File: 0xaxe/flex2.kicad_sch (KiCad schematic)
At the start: 89 parts, among them U14 MCP1824T-1802E, U6001 25MHz, U6003 NCP114ASN080T1G, U6004 ADUM141E0BRZ-RL7, U6005 +0V8, U6006 +0V8, U6007 BM1366_mode1, U6008 +0V8, U6009 +0V8, U6010 +0V8, U6011 +0V8, U6012 +0V8, U6013 +0V8, U6014 +0V8, U6015 +0V8, U6016 +0V8, U6017 +0V8, U6018 BM1366_mode1, U6019 +0V8, U6020 +0V8, U6021 BM1366_mode1, U6022 +0V8, U6024 +0V8, U6025 BM1366_mode1, U6026 +0V8

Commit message: rev1.2
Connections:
- net +5V renamed +6.5V
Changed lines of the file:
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@@
 	)
 	(symbol
-		(lib_id "power:+5V")
-		(at 86.36 175.26 0)
-		(unit 1)
-		(exclude_from_sim no)
-		(in_bom yes)
-		(on_board yes)
-		(dnp no)
-		(fields_autoplaced yes)
-		(property "Reference" "#PWR0142"
-			(at 86.36 179.07 0)
-			(effects
-				(font
-					(size 1.27 1.27)
-				)
-				(hide yes)
-			)
-		)
-		(property "Value" "+5V"
-			(at 86.36 170.18 0)
-			(effects
-				(font
-					(size 1.27 1.27)
-				)
-			)
-		)
-		(property "Footprint" ""
-			(at 86.36 175.26 0)
-			(effects
-				(font
-					(size 1.27 1.27)
-				)
-				(hide yes)
-			)
-		)
-		(property "Datasheet" ""
-			(at 86.36 175.26 0)
-			(effects
-				(font
-					(size 1.27 1.27)
-				)
-				(hide yes)
-			)
-		)
-		(property "Description" "Power symbol creates a global label with name \"+5V\""
-			(at 86.36 175.26 0)
-			(effects
-				(font
-					(size 1.27 1.27)
-				)
-				(hide yes)
-			)
-		)
-		(pin "1"
-		)
-		(instances
-			(project "0xaxe"
-				(path "/e63e39d7-6ac0-4ffd-8aa3-1841a4541b55/84d407d0-bd71-403d-bc5c-679b63d0a5ac/685a8d0d-4dc2-4a68-9e2a-a2b107c3af74"
-					(reference "#PWR0142")
-					(unit 1)
-				)
-			)
-		)
-	)
-	(symbol
 		(lib_id "Device:C")
 		(at 275.59 231.14 0)
@@
 					(unit 1)
 				)
+			)
+		)
+	)
+	(symbol
+		(lib_id "mylib7:+6.5V")
+		(at 86.36 175.26 0)
+		(unit 1)
+		(exclude_from_sim no)
+		(in_bom yes)
+		(on_board yes)
+		(dnp no)
+		(fields_autoplaced yes)
+		(property "Reference" "#PWR0142"
+			(at 86.36 179.07 0)
+			(effects
+				(font
+					(size 1.27 1.27)
+				)
+				(hide yes)
+			)
+		)
+		(property "Value" "+6.5V"
+			(at 86.36 170.18 0)
+			(effects
+				(font
+					(size 1.27 1.27)
+				)
+			)
+		)
+		(property "Footprint" ""
+			(at 86.36 175.26 0)
+			(effects
+				(font
+					(size 1.27 1.27)
+				)
+				(hide yes)
+			)
+		)
+		(property "Datasheet" ""
+			(at 86.36 175.26 0)
+			(effects
+				(font
+					(size 1.27 1.27)
+				)
+				(hide yes)
+			)
+		)
+		(property "Description" ""
+			(at 86.36 175.26 0)
+			(effects
+				(font
+					(size 1.27 1.27)
+				)
+				(hide yes)
+			)
+		)
+		(pin "1"
+		)
+		(instances
+			(project "0xaxe"
+				(path "/e63e39d7-6ac0-4ffd-8aa3-1841a4541b55/84d407d0-bd71-403d-bc5c-679b63d0a5ac/685a8d0d-4dc2-4a68-9e2a-a2b107c3af74"
+					(reference "#PWR0142")
+					(unit 1)
+				)

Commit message: op levelshifter
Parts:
- removed C6010, C6011: 100n, Capacitor_SMD:C_0805_2012Metric, symbol Device:C
- removed U6004: ADUM141E0BRZ-RL7, Package_SO:SOIC-16_3.9x9.9mm_P1.27mm, symbol Isolator:ADuM1411
- added C107: 0.1uF, Capacitor_SMD:C_0805_2012Metric, symbol Device:C
- added C108: 1uF, Capacitor_SMD:C_0805_2012Metric, symbol Device:C
- added C284, C285, C286, C287: 100pF, Capacitor_SMD:C_0805_2012Metric, symbol Device:C
- added R71, R74, R77, R78, R79, R82, R85, R86, R87: 1k, Resistor_SMD:R_0805_2012Metric, symbol Device:R
- added R72, R73, R75, R76, R80, R81, R83, R84: 10k, Resistor_SMD:R_0805_2012Metric, symbol Device:R
- added U41: TLV3544, Package_SO:SOIC-14_3.9x8.7mm_P1.27mm, symbol bitaxe:TLV3544
- renumbered C6003 to C100, C6004 to C101, C6005 to C102, C6006 to C103, C6007 to C104, C6009 to C106, C6012 to C109, C6013 to C110, C6014 to C111, C6015 to C112, C6016 to C113, C6017 to C114, C6018 to C115, C6019 to C116, C6020 to C117, C6021 to C118, C6022 to C119, C6023 to C120, C6024 to C121, C6025 to C122, C6026 to C123, C6027 to C124, C6028 to C125, C6029 to C126, C6030 to C127, C6031 to C128, C6032 to C129, C6033 to C130, C6034 to C131, C6035 to C132, C6036 to C133, C6037 to C134, C6038 to C135, C6039 to C136, C6040 to C137, C6041 to C138, C6042 to C139, C6043 to C140, C6044 to C141, C6045 to C142, C6046 to C143, C6047 to C144, C6048 to C145, C6049 to C146, C6050 to C147, C6051 to C148, C6052 to C149, C6053 to C150, C6054 to C151, C6055 to C152, C6057 to C153, C6058 to C154, C6059 to C155, C6060 to C156, C6061 to C157, C6002 to C99, R6003 to R44, R6004 to R45, R6005 to R46, R6006 to R47, U6001 to U38, U6003 to U40, U6005 to U42, U6006 to U43, U6007 to U44, U6008 to U45, U6009 to U46, U6010 to U47, U6011 to U48, U6012 to U49, U6013 to U50, U6014 to U51, U6015 to U52, U6016 to U53, U6017 to U54, U6018 to U55, U6019 to U56, U6020 to U57, U6021 to U58, U6022 to U59, U6024 to U60, U6025 to U61, U6026 to U62
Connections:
- net +6.5V: now also C107.2, C108.2, U41.4 (V+)
- net BI: now also R84.1
- net CI: now also R73.1
- net GND_1: now also R71.2, R74.2, R79.2, R82.2
- net NRSTI: now also R76.1
- net NRSTO: now also C285.2, R78.1, U41.7; no longer U44.5 (NRSTO)
- net RO: now also R87.1
- net CLKI renamed I_CLKI
- new net: R83.2, R84.2, U41.10 (+)
- new net: C287.1, R82.1, R86.2, U41.9 (-)
- new net: C286.1, R79.1, R85.2, U41.13 (-)
- new net: C286.2, R85.1, R87.2, U41.14
- new net: C285.1, R74.1, R78.2, U41.6 (-)
- new net: R80.2, R81.2, U41.12 (+)
- new net: R72.1, R73.2, U41.3 (+)
- new net: C284.1, R71.1, R77.2, U41.2 (-)
- new net: R75.2, R76.2, U41.5 (+)
- new net BI_1: C287.2, R86.1, U41.8
- new net CI_1: C284.2, R77.1, U41.1
- new net GND: C107.1, C108.1, U41.11 (V-)
- new net I_NRSTI: U44.5 (NRSTI)
- new net RO_1: R81.1
- new net VDD_1: R72.2, R75.1, R83.1
- new net VDD_REF_I: R80.1
- no-connect marks 21 -> 19
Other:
- note added: "+0V8 LDO"
- note added: "+1V8 LDO"
- note added: "25MHz Osc for CLKI"
- note added: "Levelshift of input signals to own voltage domain"
- note added: "OPAMP Bypass"
- moved on the sheet: C100, C101, C102, C103, C104, C106, C109, C110, C111, C112, C113, C114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

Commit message: General Update
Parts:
- U42, U43, U45, U46, U47, U48, U49, U50, U51, U52, U53, U54, U56, U57, U59, U60, U62: value +0V8 -> +0V8_1
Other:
- note added: "+0V8_1 LDO"
- note removed: "+0V8 LDO"
- moved on the sheet: C110, C111, C113, C114, C115, C116, C118, C119, C120, C121, C122, C124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

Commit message: fixed couple of things
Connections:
- net BI is gone; now on net BI_1: R84.1
- net CI is gone; now on net CI_1: R73.1
- net NRSTO is gone; now on net NRSTO_1: C285.2, R78.1, U41.7
- net RO is gone; now on net RO_1: R87.1
- net VDD_1 is gone; now on net +1V2_1: R72.2, R75.1, R83.1
- net BI_1: no longer C287.2, R86.1, U41.8
- net CI_1: no longer C284.2, R77.1, U41.1
- net RO_1: no longer R81.1
- net BO renamed BO_1
- net CO renamed CO_1
- net I_BI renamed I_BI_1
- net I_BI_1: now also C287.2, R86.1, U41.8
- net I_CI renamed I_CI_1
- net I_CI_1: now also C284.2, R77.1, U41.1
- net I_CLKI renamed I_CLKI_1
- net I_NRSTI renamed NRSTO_1
- net I_RO renamed I_RO_1
- net I_RO_1: now also R81.1
- net NRSTI renamed NRSTI_1
- net RI renamed RI_1
- net VDD_REF_I renamed VDD_REF_I_1
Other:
- moved on the sheet: C100, C101, C103, C107, C108, C110, C111, C113, C114, C115, C116, C117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

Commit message: Layout update
Layout with OP
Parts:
- removed R71, R74, R77, R78, R79, R82, R85, R86, R87: 1k, Resistor_SMD:R_0805_2012Metric, symbol Device:R
- removed R72, R73, R75, R76, R80, R81, R83, R84: 10k, Resistor_SMD:R_0805_2012Metric, symbol Device:R
- added RN5, RN6, RN7, RN8: 10k, EXB-28V103JX:EXB28V_PAN, symbol Device:R_Network04_Split
- U44, U55, U58, U61: footprint qaxe:BM1366 -> bitvein:BM1366
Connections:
- net +1V2_1: now also RN5.8 (R4.2), RN6.1 (R1), RN8.4 (R2.2)
- net BI_1: now also RN8.5 (R2.2)
- net CI_1: now also RN5.1 (R1)
- net GND_1: now also RN5.5 (R2.2), RN6.4 (R2.2), RN7.4 (R2.2), RN8.1 (R1)
- net I_BI_1: now also RN8.8 (R4.2)
- net I_CI_1: now also RN5.4 (R2.2)
- net I_RO_1: now also RN7.8 (R4.2)
- net NRSTI_1: now also RN6.8 (R4.2)
- net NRSTO_1: now also RN6.5 (R2.2)
- net RO_1: now also C286.2, U41.14, RN7.5 (R2.2)
- net VDD_REF_I_1: now also RN7.1 (R1)
- net at U41.10 (+): now also RN8.3 (R2.2), RN8.6 (R3.2)
- net at C287.1, U41.9 (-): now also RN8.2 (R1.2), RN8.7 (R2.2)
- net at C286.1, U41.13 (-): now also RN7.3 (R2.2), RN7.6 (R3.2)
- net at C285.1, U41.6 (-): now also RN6.3 (R2.2), RN6.6 (R3.2)
- net at U41.12 (+): now also RN7.2 (R1.2), RN7.7 (R2.2)
- net at U41.3 (+): now also RN5.2 (R1.2), RN5.7 (R2.2)
- net at C284.1, U41.2 (-): now also RN5.3 (R2.2), RN5.6 (R3.2)
- net at U41.5 (+): now also RN6.2 (R1.2), RN6.7 (R2.2)

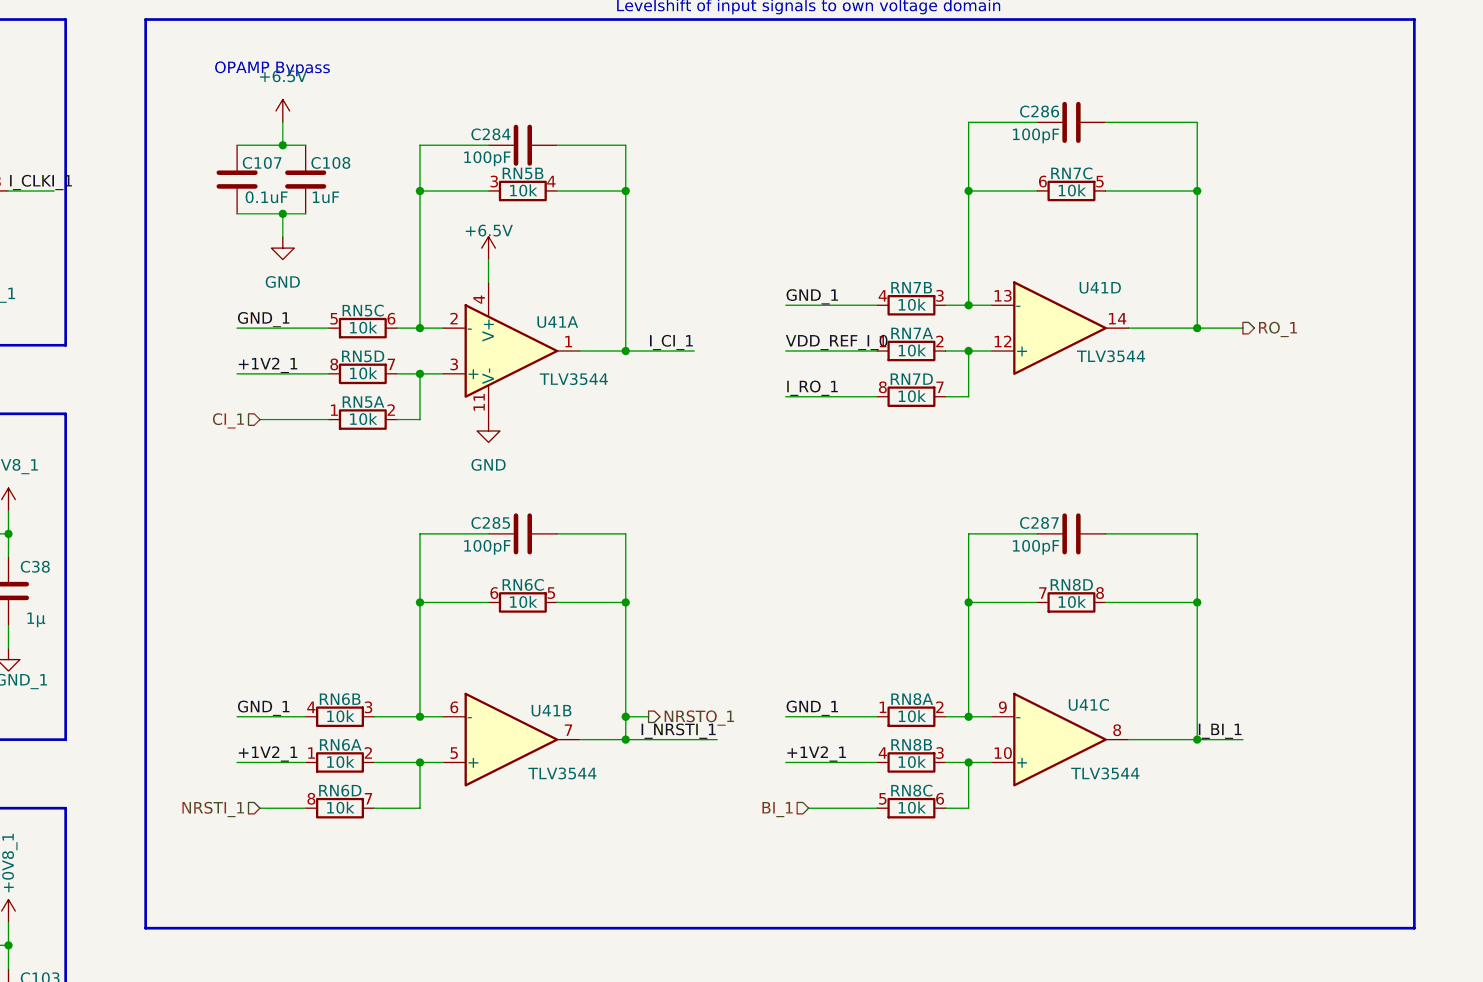
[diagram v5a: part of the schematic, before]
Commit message: fixed level shifter, added optional headers for future extensions
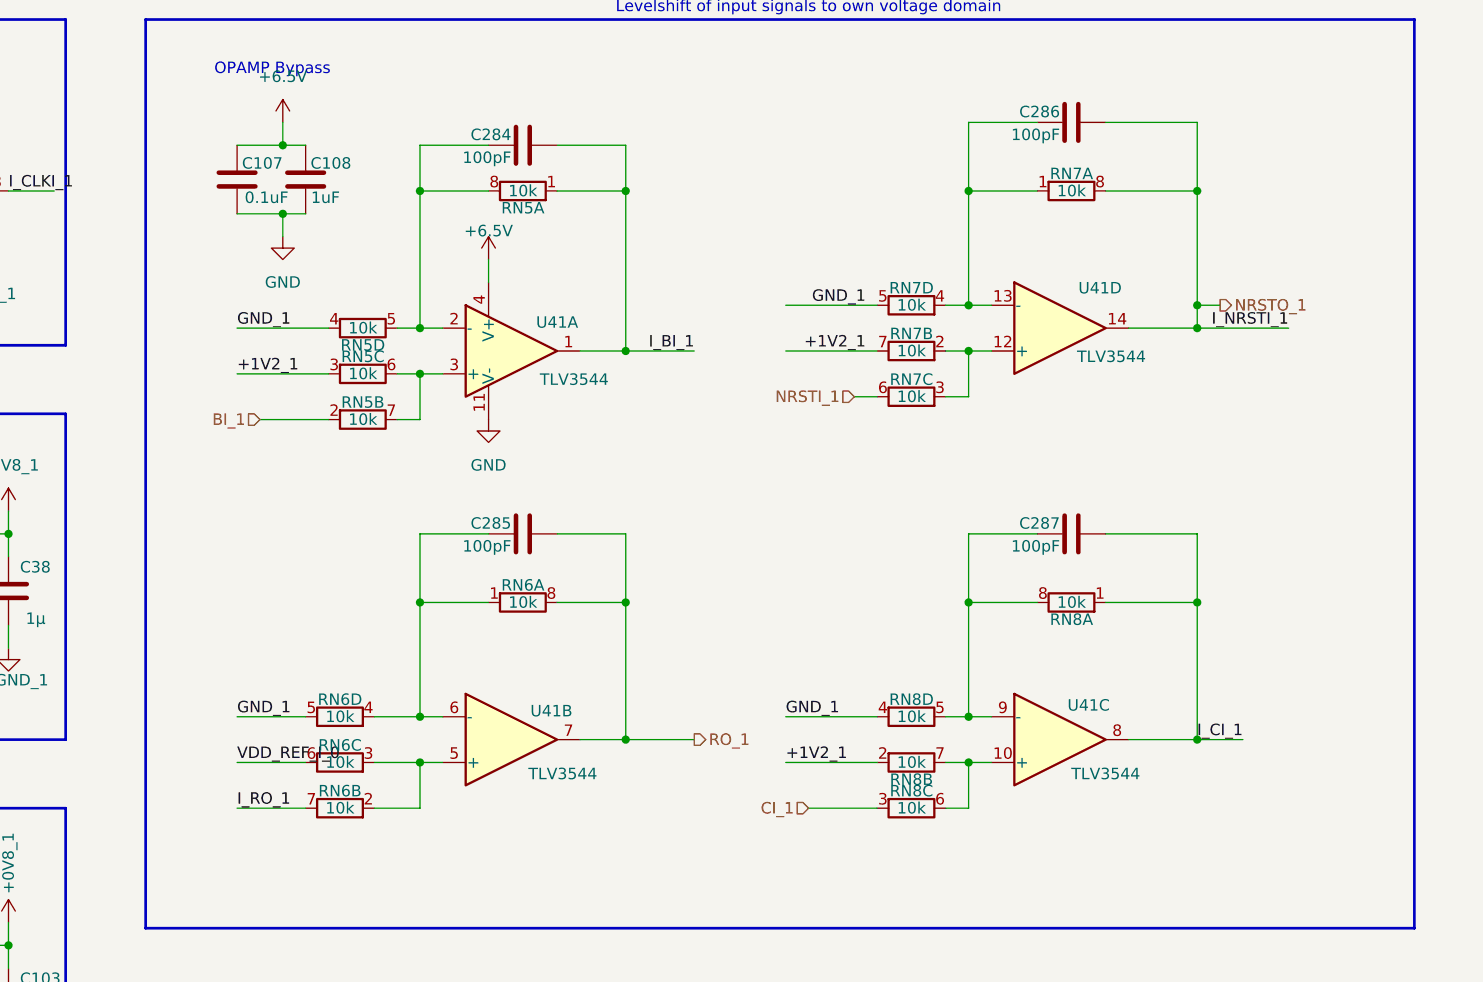
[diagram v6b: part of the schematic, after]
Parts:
- RN5, RN6, RN7, RN8: footprint EXB-28V103JX:EXB28V_PAN -> Resistor_SMD:R_Array_Convex_4x0603; symbol Device:R_Network04_Split -> mylib7:R_Network04_Split_SMD
- U44, U55, U58, U61: footprint bitvein:BM1366 -> myfootprints:BM1366-user1-soldermask
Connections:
- net +1V2_1: now also RN5.3 (R3.1), RN7.7 (R2.2), RN8.2 (R2.1); no longer RN5.8 (R4.2), RN6.1 (R1), RN8.4 (R2.2)
- net BI_1: now also RN5.2 (R2.1); no longer RN8.5 (R2.2)
- net CI_1: now also RN8.3 (R3.1); no longer RN5.1 (R1)
- net GND_1: now also RN5.4 (R4.1), RN6.5 (R4.2), RN7.5 (R4.2), RN8.4 (R4.1); no longer RN5.5 (R2.2), RN6.4 (R2.2), RN7.4 (R2.2), RN8.1 (R1)
- net I_BI_1: now also C284.2, RN5.1 (R1.1), U41.1; no longer C287.2, RN8.8 (R4.2), U41.8
- net I_CI_1: now also C287.2, RN8.1 (R1.1), U41.8; no longer C284.2, RN5.4 (R2.2), U41.1
- net I_RO_1: now also RN6.7 (R2.2); no longer RN7.8 (R4.2)
- net NRSTI_1: now also RN7.6 (R3.2); no longer RN6.8 (R4.2)
- net NRSTO_1: now also C286.2, RN7.8 (R1.2), U41.14; no longer C285.2, RN6.5 (R2.2), U41.7
- net RO_1: now also C285.2, RN6.8 (R1.2), U41.7; no longer C286.2, RN7.5 (R2.2), U41.14
- net VDD_REF_I_1: now also RN6.6 (R3.2); no longer RN7.1 (R1)
- net at RN8.6 (R3.2), U41.10 (+): now also RN8.7 (R2.2); no longer RN8.3 (R2.2)
- net at C287.1, U41.9 (-): now also RN8.5 (R4.2), RN8.8 (R1.2); no longer RN8.2 (R1.2), RN8.7 (R2.2)
- net at C285.1, U41.6 (-): now also RN6.1 (R1.1), RN6.4 (R4.1); no longer RN6.3 (R2.2), RN6.6 (R3.2)
- net at C286.1, U41.13 (-): now also RN7.1 (R1.1), RN7.4 (R4.1); no longer RN7.3 (R2.2), RN7.6 (R3.2)
- net at C284.1, U41.2 (-): now also RN5.5 (R4.2), RN5.8 (R1.2); no longer RN5.3 (R2.2), RN5.6 (R3.2)
- new net: RN6.2 (R2.1), RN6.3 (R3.1), U41.5 (+)
- new net: RN7.2 (R2.1), RN7.3 (R3.1), U41.12 (+)
- new net: RN5.6 (R3.2), RN5.7 (R2.2), U41.3 (+)
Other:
- moved on the sheet: RN5A, RN5B, RN5C, RN5D, RN6A, RN6B, RN6C, RN6D, RN7A, RN7B, RN7C, RN7D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

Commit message: updated BOM and gerbers
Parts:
- C107: value 0.1uF -> 100n
- C108: value 1uF -> 1µ
- C284, C285, C286, C287: value 100pF -> 100p
- RN5, RN6, RN7, RN8: value 10k -> 10k-CX; Distributor (none) -> D; Manufacturer (none) -> CAY16-1002F4LF; OrderNr (none) -> CAY16-1002F4LFCT-ND
- U41: value TLV3544 -> TLV9154; Distributor (none) -> D; Manufacturer (none) -> TLV9154IDR; OrderNr (none) -> 296-TLV9154IDRCT-ND
